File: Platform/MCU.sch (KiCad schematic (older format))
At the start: 32 parts, among them J10 Conn_01x05, J11 Aardvark Header SPI, J12 Aardvark Header I2C, J13 ESP8266_CONN, J14 Aardvark Header I2C, J4 Conn_01x05, J6 Debug Hdr, J7 Conn_01x05, U3 ATSAMD21E16B-M

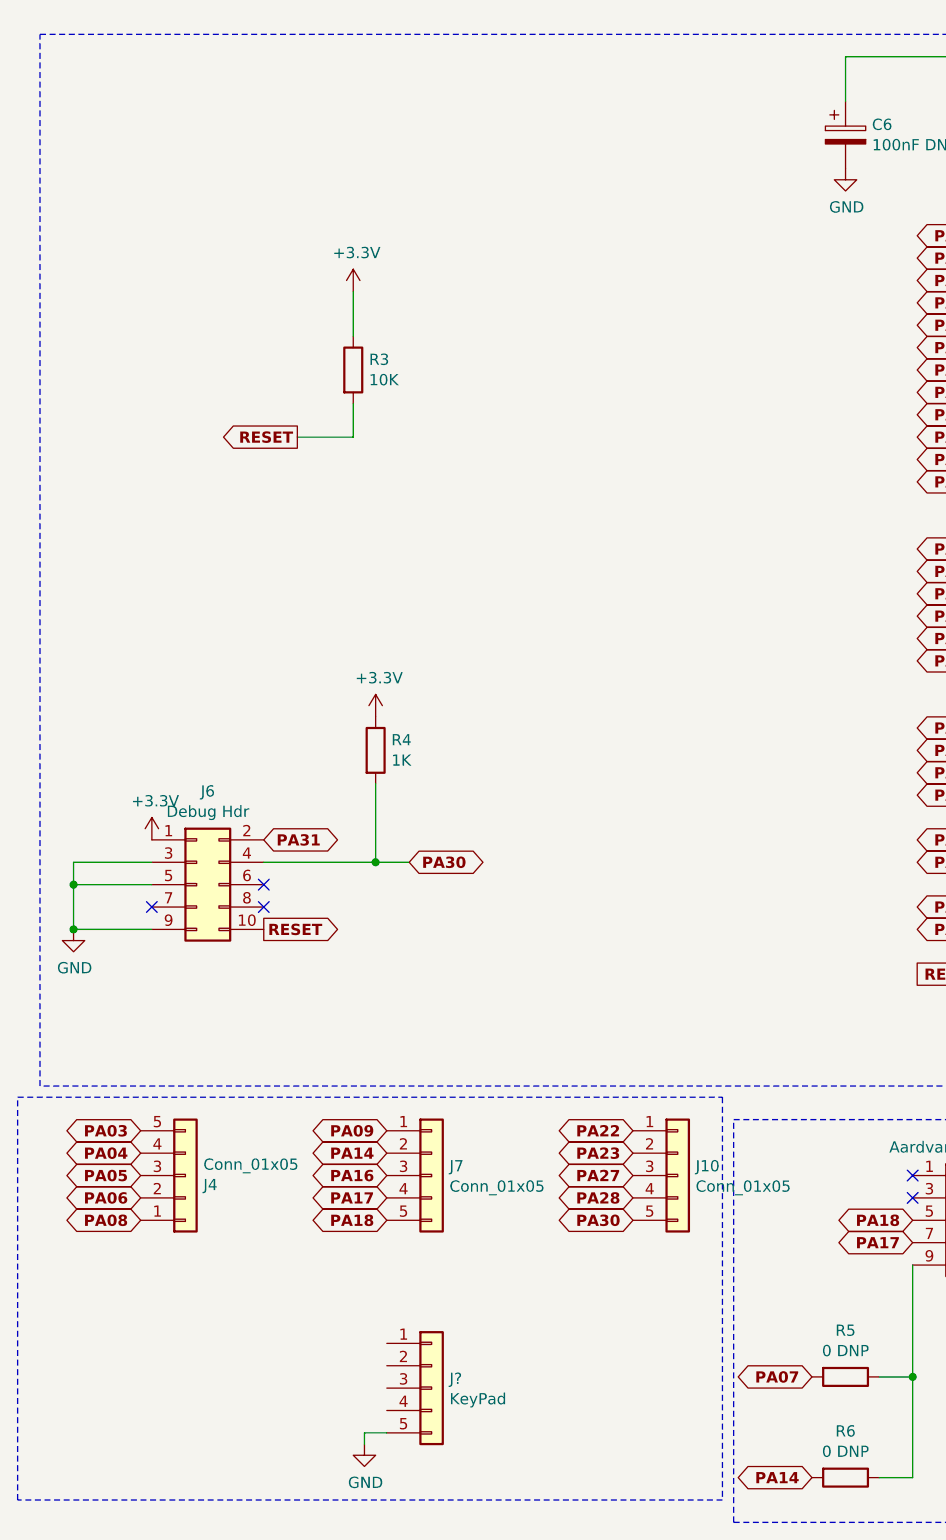
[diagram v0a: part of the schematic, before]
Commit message: Updated platform schematic.
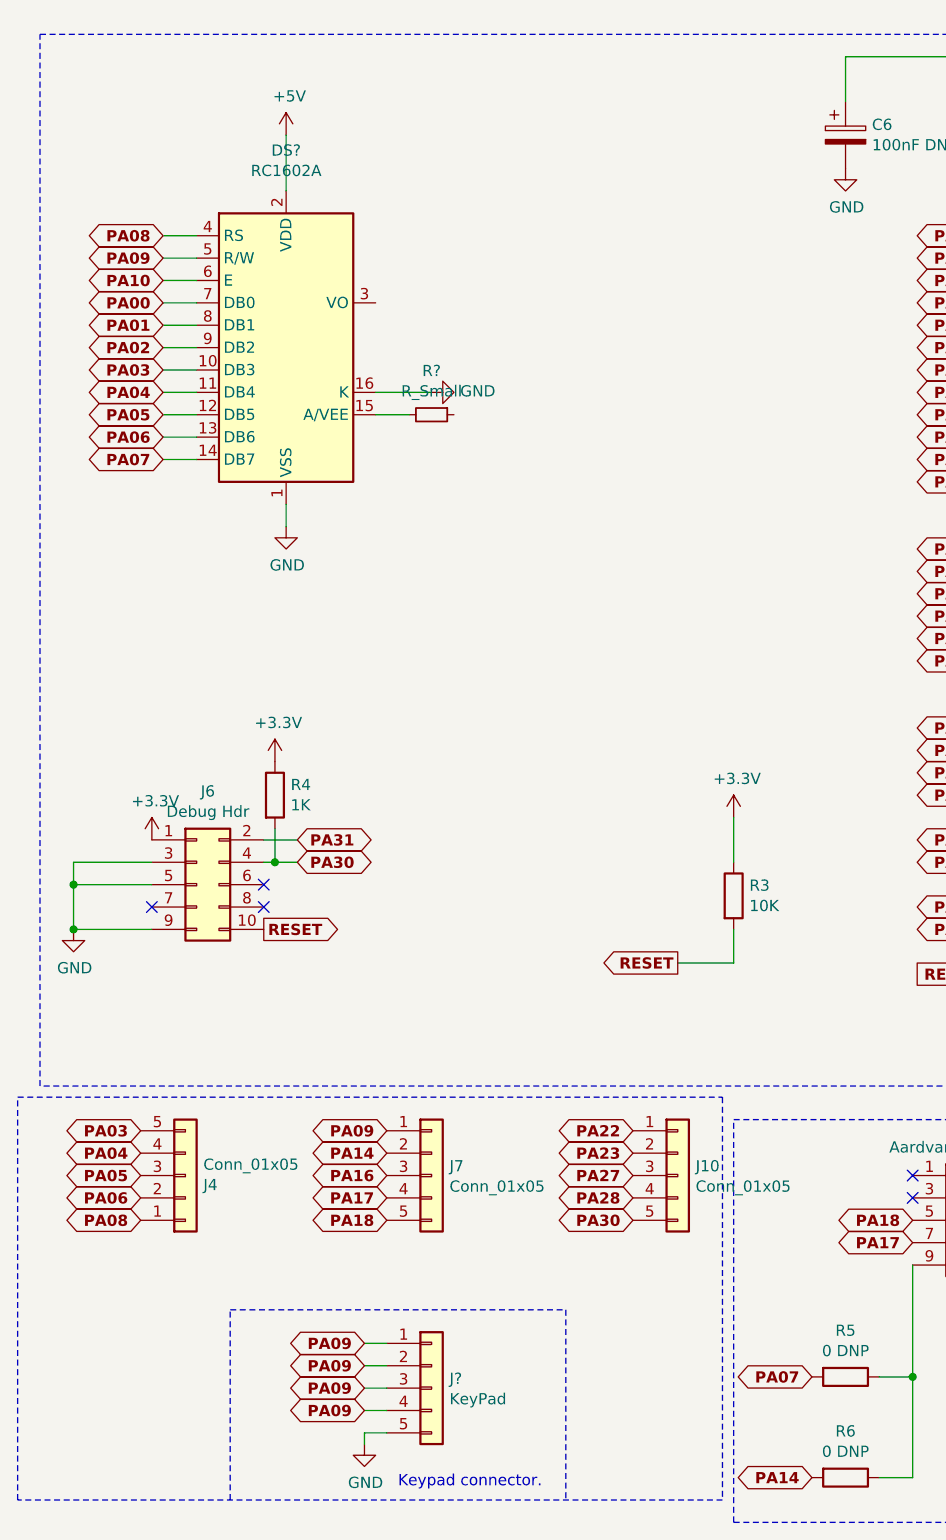
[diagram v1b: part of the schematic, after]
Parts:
- added DS?: RC1602A, Display:HY1602E, symbol Display_Character:RC1602A
- added R?: R_Small, symbol Device:R_Small
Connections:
- net +5V: now also DS?.2 (VDD)
- net GND: now also DS?.1 (VSS), DS?.16 (K)
- net PA00: now also DS?.7 (DB0)
- net PA01: now also DS?.8 (DB1)
- net PA02: now also DS?.9 (DB2)
- net PA03: now also DS?.10 (DB3)
- net PA04: now also DS?.11 (DB4)
- net PA05: now also DS?.12 (DB5)
- net PA06: now also DS?.13 (DB6)
- net PA07: now also DS?.14 (DB7)
- net PA08: now also DS?.4 (RS)
- net PA09: now also J?.1 (Pin_1), J?.2 (Pin_2), J?.3 (Pin_3), J?.4 (Pin_4), DS?.5 (R/W)
- net PA10: now also DS?.6 (E)
- new net: DS?.15 (A/VEE), R?.2
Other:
- note added: "Keypad connector."
- moved on the sheet: R3, R4
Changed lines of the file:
@@
 L power:+3.3V #PWR015
 U 1 1 5FAA344E
-P 2050 2100
-F 0 "#PWR015" H 2050 1950 50  0001 C CNN
-F 1 "+3.3V" H 2065 2273 50  0000 C CNN
-F 2 "" H 2050 2100 50  0001 C CNN
-F 3 "" H 2050 2100 50  0001 C CNN
-	1    2050 2100
-	1    0    0    -1
-$EndComp
-Text GLabel 1800 2750 0    50   Output ~ 10
+P 3750 4450
+F 0 "#PWR015" H 3750 4300 50  0001 C CNN
+F 1 "+3.3V" H 3765 4623 50  0000 C CNN
+F 2 "" H 3750 4450 50  0001 C CNN
+F 3 "" H 3750 4450 50  0001 C CNN
+	1    3750 4450
+	1    0    0    -1
+$EndComp
+Text GLabel 3500 5100 0    50   Output ~ 10
 RESET
 $Comp
 L Device:R R3
 U 1 1 5FAA5047
-P 2050 2450
-F 0 "R3" H 2120 2496 50  0000 L CNN
-F 1 "10K" H 2120 2405 50  0000 L CNN
-F 2 "" V 1980 2450 50  0001 C CNN
-F 3 "~" H 2050 2450 50  0001 C CNN
-	1    2050 2450
-	1    0    0    -1
-$EndComp
-Wire Wire Line
-	2050 2100 2050 2300
-Wire Wire Line
-	2050 2600 2050 2750
-Wire Wire Line
-	2050 2750 1800 2750
-Text GLabel 2300 4650 2    50   BiDi ~ 10
+P 3750 4800
+F 0 "R3" H 3820 4846 50  0000 L CNN
+F 1 "10K" H 3820 4755 50  0000 L CNN
+F 2 "" V 3680 4800 50  0001 C CNN
+F 3 "~" H 3750 4800 50  0001 C CNN
+	1    3750 4800
+	1    0    0    -1
+$EndComp
+Wire Wire Line
+	3750 4450 3750 4650
+Wire Wire Line
+	3750 4950 3750 5100
+Wire Wire Line
+	3750 5100 3500 5100
+Text GLabel 1800 4650 2    50   BiDi ~ 10
 PA30
-Text GLabel 1650 4550 2    50   BiDi ~ 10
+Text GLabel 1800 4550 2    50   BiDi ~ 10
 PA31
 $Comp
@@
 L Device:R R4
 U 1 1 5FB6E9FD
-P 2150 4150
-F 0 "R4" H 2220 4196 50  0000 L CNN
-F 1 "1K" H 2220 4105 50  0000 L CNN
-F 2 "" V 2080 4150 50  0001 C CNN
-F 3 "~" H 2150 4150 50  0001 C CNN
-	1    2150 4150
-	1    0    0    -1
-$EndComp
-Wire Wire Line
-	2300 4650 2150 4650
-Wire Wire Line
-	2150 4300 2150 4650
-Connection ~ 2150 4650
-Wire Wire Line
-	2150 4650 1650 4650
+P 1700 4350
+F 0 "R4" H 1770 4396 50  0000 L CNN
+F 1 "1K" H 1770 4305 50  0000 L CNN
+F 2 "" V 1630 4350 50  0001 C CNN
+F 3 "~" H 1700 4350 50  0001 C CNN
+	1    1700 4350
+	1    0    0    -1
+$EndComp
+Wire Wire Line
+	1800 4650 1700 4650
+Wire Wire Line
+	1700 4500 1700 4650
+Connection ~ 1700 4650
+Wire Wire Line
+	1700 4650 1650 4650
 $Comp
 L power:+3.3V #PWR016
 U 1 1 5FB75E85
-P 2150 4000
-F 0 "#PWR016" H 2150 3850 50  0001 C CNN
-F 1 "+3.3V" H 2165 4173 50  0000 C CNN
-F 2 "" H 2150 4000 50  0001 C CNN
-F 3 "" H 2150 4000 50  0001 C CNN
-	1    2150 4000
+P 1700 4200
+F 0 "#PWR016" H 1700 4050 50  0001 C CNN
+F 1 "+3.3V" H 1715 4373 50  0000 C CNN
+F 2 "" H 1700 4200 50  0001 C CNN
+F 3 "" H 1700 4200 50  0001 C CNN
+	1    1700 4200
 	1    0    0    -1
 $EndComp
@@
 Wire Wire Line
 	4250 1050 4250 1250
+Text GLabel 2100 6800 0    50   BiDi ~ 10
+PA09
+Text GLabel 2100 6900 0    50   BiDi ~ 10
+PA09
+Text GLabel 2100 7000 0    50   BiDi ~ 10
+PA09
+Text GLabel 2100 7100 0    50   BiDi ~ 10
+PA09
+Wire Wire Line
+	2200 7100 2100 7100
+Wire Wire Line
+	2100 7000 2200 7000
+Wire Wire Line
+	2200 6900 2100 6900
+Wire Wire Line
+	2100 6800 2200 6800
+Wire Notes Line
+	3000 6650 3000 7500
+Wire Notes Line
+	1500 7500 1500 6650
+Wire Notes Line
+	1500 6650 3000 6650
+Text Notes 2250 7450 0    50   ~ 0
+Keypad connector.
+$Comp
+L Display_Character:RC1602A DS?
+U 1 1 6019A893
+P 1750 2350
+F 0 "DS?" H 1750 3231 50  0000 C CNN
+F 1 "RC1602A" H 1750 3140 50  0000 C CNN
+F 2 "Display:HY1602E" H 1750 1450 50  0001 C CIN
+F 3 "http://www.icbank.com/data/ICBShop/board/HY1602E.pdf" H 1950 2450 50  0001 C CNN
+	1    1750 2350
+	1    0    0    -1
+$EndComp
+Wire Wire Line
+	1800 4550 1650 4550
+Text GLabel 1200 2150 0    50   BiDi ~ 10
+PA00
+Text GLabel 1200 2250 0    50   BiDi ~ 10
+PA01
+Text GLabel 1200 2350 0    50   BiDi ~ 10
+PA02
+Text GLabel 1200 2450 0    50   BiDi ~ 10
+PA03
+Text GLabel 1200 2550 0    50   BiDi ~ 10
+PA04
+Text GLabel 1200 2650 0    50   BiDi ~ 10
+PA05
+Text GLabel 1200 2750 0    50   BiDi ~ 10
+PA06
+Text GLabel 1200 2850 0    50   BiDi ~ 10
+PA07
+Wire Wire Line
+	1200 2150 1350 2150
+Wire Wire Line
+	1350 2250 1200 2250
+Wire Wire Line
+	1200 2350 1350 2350
+Wire Wire Line
+	1350 2450 1200 2450
+Wire Wire Line
+	1200 2550 1350 2550
+Wire Wire Line
+	1350 2650 1200 2650
+Wire Wire Line
+	1200 2750 1350 2750
+Wire Wire Line
+	1350 2850 1200 2850
+$Comp
+L power:+5V #PWR?
+U 1 1 601E129D
+P 1750 1400
+F 0 "#PWR?" H 1750 1250 50  0001 C CNN
+F 1 "+5V" H 1765 1573 50  0000 C CNN
+F 2 "" H 1750 1400 50  0001 C CNN
+F 3 "" H 1750 1400 50  0001 C CNN
+	1    1750 1400
+	1    0    0    -1
+$EndComp
+$Comp
+L power:GND #PWR?
+U 1 1 601E5E6B
+P 1750 3150
+F 0 "#PWR?" H 1750 2900 50  0001 C CNN
+F 1 "GND" H 1755 2977 50  0000 C CNN
+F 2 "" H 1750 3150 50  0001 C CNN
+F 3 "" H 1750 3150 50  0001 C CNN
+	1    1750 3150
+	1    0    0    -1
+$EndComp
+Wire Wire Line
+	1750 3150 1750 3050
+Wire Wire Line
+	1750 1400 1750 1650
+Text GLabel 1200 1850 0    50   BiDi ~ 10
+PA08
+Text GLabel 1200 1950 0    50   BiDi ~ 10
+PA09
+Text GLabel 1200 2050 0    50   BiDi ~ 10
+PA10
+Wire Wire Line
+	1350 2050 1200 2050
+Wire Wire Line
+	1200 1950 1350 1950
+Wire Wire Line
+	1350 1850 1200 1850
+$Comp
+L Device:R_Small R?
+U 1 1 6020D43B
+P 2400 2650
+F 0 "R?" V 2204 2650 50  0000 C CNN
+F 1 "R_Small" V 2295 2650 50  0000 C CNN
+F 2 "" H 2400 2650 50  0001 C CNN
+F 3 "~" H 2400 2650 50  0001 C CNN
+	1    2400 2650
+	0    1    1    0
+$EndComp
+$Comp
+L power:GND #PWR?
+U 1 1 60207B70
+P 2400 2550
+F 0 "#PWR?" H 2400 2300 50  0001 C CNN
+F 1 "GND" V 2405 2422 50  0000 R CNN
+F 2 "" H 2400 2550 50  0001 C CNN
+F 3 "" H 2400 2550 50  0001 C CNN
+	1    2400 2550
+	0    -1   -1   0
+$EndComp
+Wire Wire Line
+	2150 2550 2400 2550
+Wire Wire Line
+	2300 2650 2150 2650
 $EndSCHEMATC

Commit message: Updated the schematic.
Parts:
- added Q?: BC547, Package_TO_SOT_THT:TO-92_Inline, symbol Transistor_BJT:BC547
- added R?: R_Small, symbol Device:R_Small
- added RV?: R_POT, symbol Device:R_POT
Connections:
- net +5V: now also R?.2, RV?.3
- net GND: now also RV?.1
- net at DS?.15 (A/VEE): now also Q?.3 (E); no longer R?.2
- net at DS?.3 (VO): now also RV?.2
- new net: Q?.1 (C), R?.1
- new net: Q?.2 (B), R?.2
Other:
- moved on the sheet: R?
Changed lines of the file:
@@
 	1750 3150 1750 3050
 Wire Wire Line
-	1750 1400 1750 1650
+	1750 1400 1750 1550
 Text GLabel 1200 1850 0    50   BiDi ~ 10
 PA08
@@
 L Device:R_Small R?
 U 1 1 6020D43B
-P 2400 2650
-F 0 "R?" V 2204 2650 50  0000 C CNN
-F 1 "R_Small" V 2295 2650 50  0000 C CNN
-F 2 "" H 2400 2650 50  0001 C CNN
-F 3 "~" H 2400 2650 50  0001 C CNN
-	1    2400 2650
+P 3550 2350
+F 0 "R?" V 3450 2350 50  0000 C CNN
+F 1 "R_Small" V 3650 2350 50  0000 C CNN
+F 2 "" H 3550 2350 50  0001 C CNN
+F 3 "~" H 3550 2350 50  0001 C CNN
+	1    3550 2350
 	0    1    1    0
 $EndComp
@@
 L power:GND #PWR?
 U 1 1 60207B70
-P 2400 2550
-F 0 "#PWR?" H 2400 2300 50  0001 C CNN
-F 1 "GND" V 2405 2422 50  0000 R CNN
-F 2 "" H 2400 2550 50  0001 C CNN
-F 3 "" H 2400 2550 50  0001 C CNN
-	1    2400 2550
-	0    -1   -1   0
+P 2350 2350
+F 0 "#PWR?" H 2350 2100 50  0001 C CNN
+F 1 "GND" H 2550 2350 50  0000 R CNN
+F 2 "" H 2350 2350 50  0001 C CNN
+F 3 "" H 2350 2350 50  0001 C CNN
+	1    2350 2350
+	1    0    0    -1
+$EndComp
+$Comp
+L power:+5V #PWR?
+U 1 1 601A2CF8
+P 3000 1700
+F 0 "#PWR?" H 3000 1550 50  0001 C CNN
+F 1 "+5V" H 3015 1873 50  0000 C CNN
+F 2 "" H 3000 1700 50  0001 C CNN
+F 3 "" H 3000 1700 50  0001 C CNN
+	1    3000 1700
+	1    0    0    -1
+$EndComp
+$Comp
+L Device:R_POT RV?
+U 1 1 601A87D3
+P 2350 2150
+F 0 "RV?" H 2280 2104 50  0000 R CNN
+F 1 "R_POT" H 2280 2195 50  0000 R CNN
+F 2 "" H 2350 2150 50  0001 C CNN
+F 3 "~" H 2350 2150 50  0001 C CNN
+	1    2350 2150
+	-1   0    0    1
 $EndComp
 Wire Wire Line
-	2150 2550 2400 2550
+	2200 2150 2150 2150
 Wire Wire Line
-	2300 2650 2150 2650
+	2350 2000 2350 1550
+Wire Wire Line
+	2350 1550 1750 1550
+Connection ~ 1750 1550
+Wire Wire Line
+	1750 1550 1750 1650
+Wire Wire Line
+	2350 2350 2350 2300
+Wire Wire Line
+	2350 2350 2250 2350
+Wire Wire Line
+	2250 2350 2250 2550
+Wire Wire Line
+	2250 2550 2150 2550
+Connection ~ 2350 2350
+$Comp
+L Transistor_BJT:BC547 Q?
+U 1 1 601C0547
+P 3100 2350
+F 0 "Q?" H 3291 2396 50  0000 L CNN
+F 1 "BC547" H 3291 2305 50  0000 L CNN
+F 2 "Package_TO_SOT_THT:TO-92_Inline" H 3300 2275 50  0001 L CIN
+F 3 "https://www.onsemi.com/pub/Collateral/BC550-D.pdf" H 3100 2350 50  0001 L CNN
+	1    3100 2350
+	-1   0    0    -1
+$EndComp
+$Comp
+L Device:R_Small R?
+U 1 1 601C3595
+P 3000 1950
+F 0 "R?" V 2900 1950 50  0000 C CNN
+F 1 "R_Small" V 3100 1950 50  0000 C CNN
+F 2 "" H 3000 1950 50  0001 C CNN
+F 3 "~" H 3000 1950 50  0001 C CNN
+	1    3000 1950
+	-1   0    0    1
+$EndComp
+Wire Wire Line
+	3000 2550 3000 2650
+Wire Wire Line
+	3000 2650 2150 2650
+Wire Wire Line
+	3000 2150 3000 2050
+Wire Wire Line
+	3000 1700 3000 1850
+Wire Wire Line
+	3300 2350 3450 2350
 $EndSCHEMATC

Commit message: Updated the schematic.
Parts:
- added C?: C_Small, symbol Device:C_Small
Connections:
- net GND: now also C?.2
- net PA09: no longer J?.2 (Pin_2), J?.3 (Pin_3), J?.4 (Pin_4)
- net PA14: now also J?.2 (Pin_2)
- net PA16: now also J?.3 (Pin_3)
- net PA17: now also J?.4 (Pin_4)
- net PA28: now also R?.1
- net RESET: now also C?.1
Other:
- moved on the sheet: R3
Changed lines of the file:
@@
 L power:+3.3V #PWR015
 U 1 1 5FAA344E
-P 3750 4450
-F 0 "#PWR015" H 3750 4300 50  0001 C CNN
-F 1 "+3.3V" H 3765 4623 50  0000 C CNN
-F 2 "" H 3750 4450 50  0001 C CNN
-F 3 "" H 3750 4450 50  0001 C CNN
-	1    3750 4450
-	1    0    0    -1
-$EndComp
-Text GLabel 3500 5100 0    50   Output ~ 10
+P 3200 3500
+F 0 "#PWR015" H 3200 3350 50  0001 C CNN
+F 1 "+3.3V" H 3215 3673 50  0000 C CNN
+F 2 "" H 3200 3500 50  0001 C CNN
+F 3 "" H 3200 3500 50  0001 C CNN
+	1    3200 3500
+	-1   0    0    -1
+$EndComp
+Text GLabel 3450 4150 2    50   Output ~ 10
 RESET
 $Comp
 L Device:R R3
 U 1 1 5FAA5047
-P 3750 4800
-F 0 "R3" H 3820 4846 50  0000 L CNN
-F 1 "10K" H 3820 4755 50  0000 L CNN
-F 2 "" V 3680 4800 50  0001 C CNN
-F 3 "~" H 3750 4800 50  0001 C CNN
-	1    3750 4800
-	1    0    0    -1
-$EndComp
-Wire Wire Line
-	3750 4450 3750 4650
-Wire Wire Line
-	3750 4950 3750 5100
-Wire Wire Line
-	3750 5100 3500 5100
+P 3200 3850
+F 0 "R3" H 3270 3896 50  0000 L CNN
+F 1 "10K" H 3270 3805 50  0000 L CNN
+F 2 "" V 3130 3850 50  0001 C CNN
+F 3 "~" H 3200 3850 50  0001 C CNN
+	1    3200 3850
+	-1   0    0    -1
+$EndComp
+Wire Wire Line
+	3200 3500 3200 3700
+Wire Wire Line
+	3200 4000 3200 4150
+Wire Wire Line
+	3200 4150 3450 4150
 Text GLabel 1800 4650 2    50   BiDi ~ 10
 PA30
@@
 PA09
 Text GLabel 2100 6900 0    50   BiDi ~ 10
-PA09
+PA14
 Text GLabel 2100 7000 0    50   BiDi ~ 10
-PA09
+PA16
 Text GLabel 2100 7100 0    50   BiDi ~ 10
-PA09
+PA17
 Wire Wire Line
 	2200 7100 2100 7100
@@
 Wire Wire Line
 	3300 2350 3450 2350
+$Comp
+L Device:C_Small C?
+U 1 1 601CEA06
+P 3200 4400
+F 0 "C?" H 3292 4446 50  0000 L CNN
+F 1 "C_Small" H 3292 4355 50  0000 L CNN
+F 2 "" H 3200 4400 50  0001 C CNN
+F 3 "~" H 3200 4400 50  0001 C CNN
+	1    3200 4400
+	1    0    0    -1
+$EndComp
+$Comp
+L power:GND #PWR?
+U 1 1 601CEDC7
+P 3200 4650
+F 0 "#PWR?" H 3200 4400 50  0001 C CNN
+F 1 "GND" H 3205 4477 50  0000 C CNN
+F 2 "" H 3200 4650 50  0001 C CNN
+F 3 "" H 3200 4650 50  0001 C CNN
+	1    3200 4650
+	1    0    0    -1
+$EndComp
+Wire Wire Line
+	3200 4650 3200 4500
+Wire Wire Line
+	3200 4300 3200 4150
+Connection ~ 3200 4150
+Text GLabel 3750 2350 2    50   BiDi ~ 10
+PA28
+Wire Wire Line
+	3750 2350 3650 2350
 $EndSCHEMATC
